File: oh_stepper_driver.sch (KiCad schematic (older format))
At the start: 22 parts, among them P2 CONN_01X02, P3 CONN_01X02, SW1 BOOT_MODE, SW2 RST, U2 STM32F446RCTx, X1 ABM8G

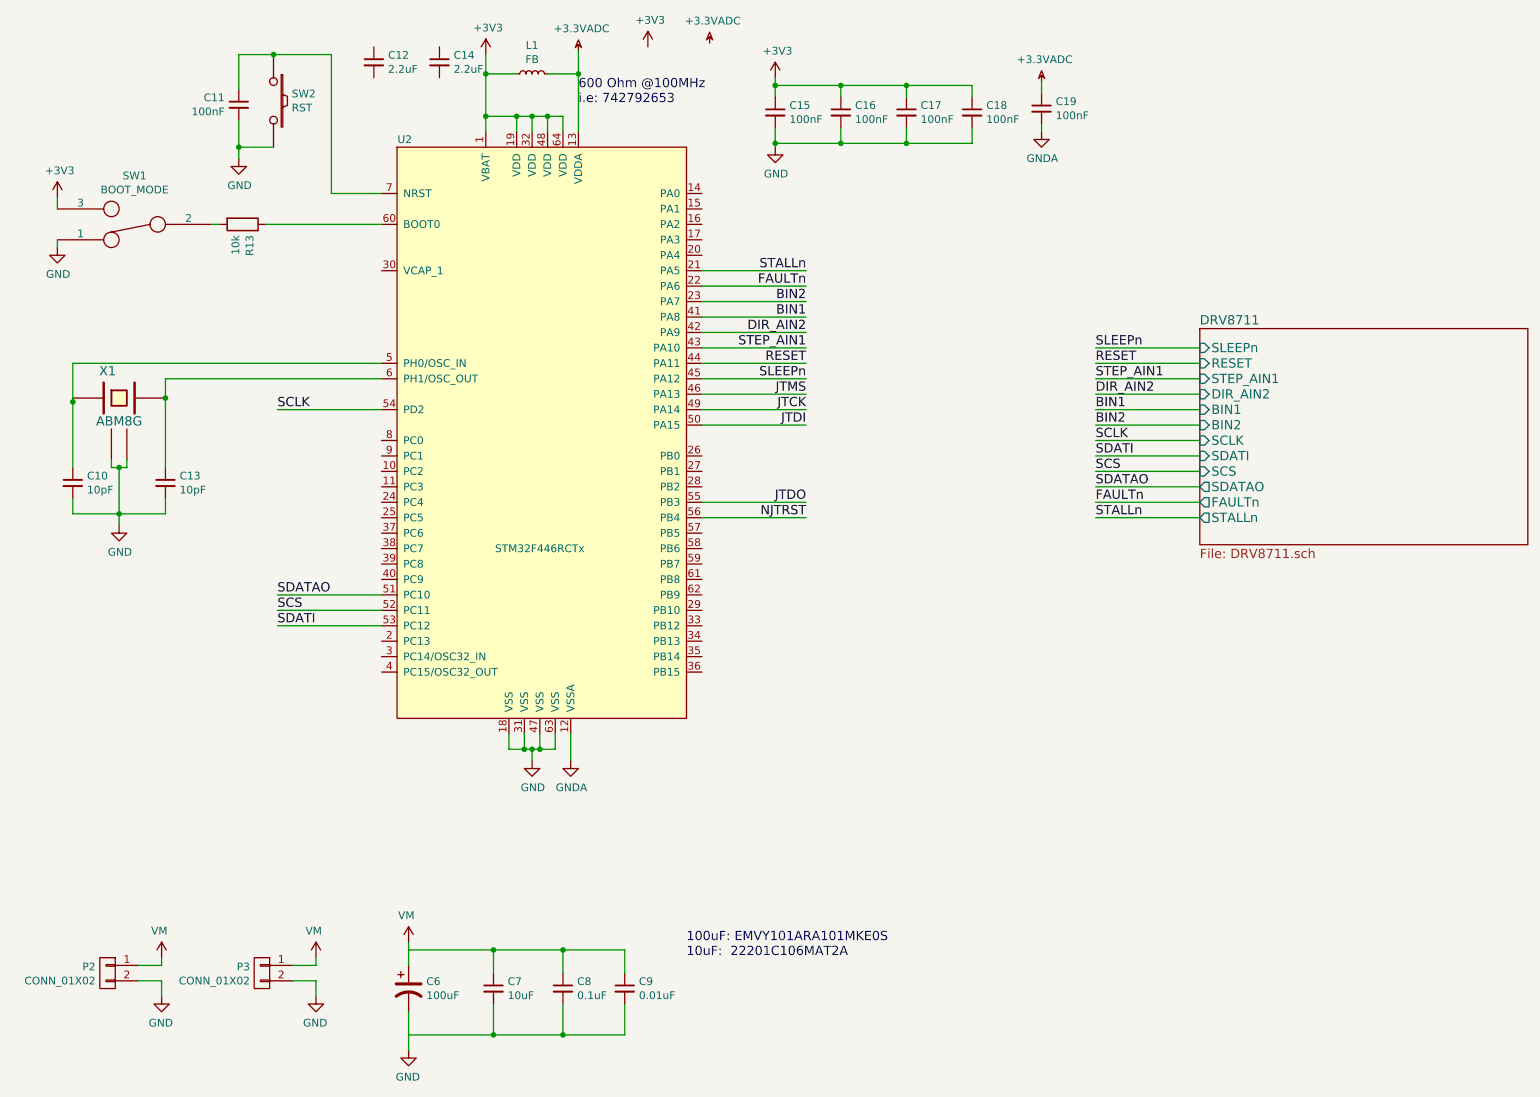
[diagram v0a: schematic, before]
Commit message: routing FETs
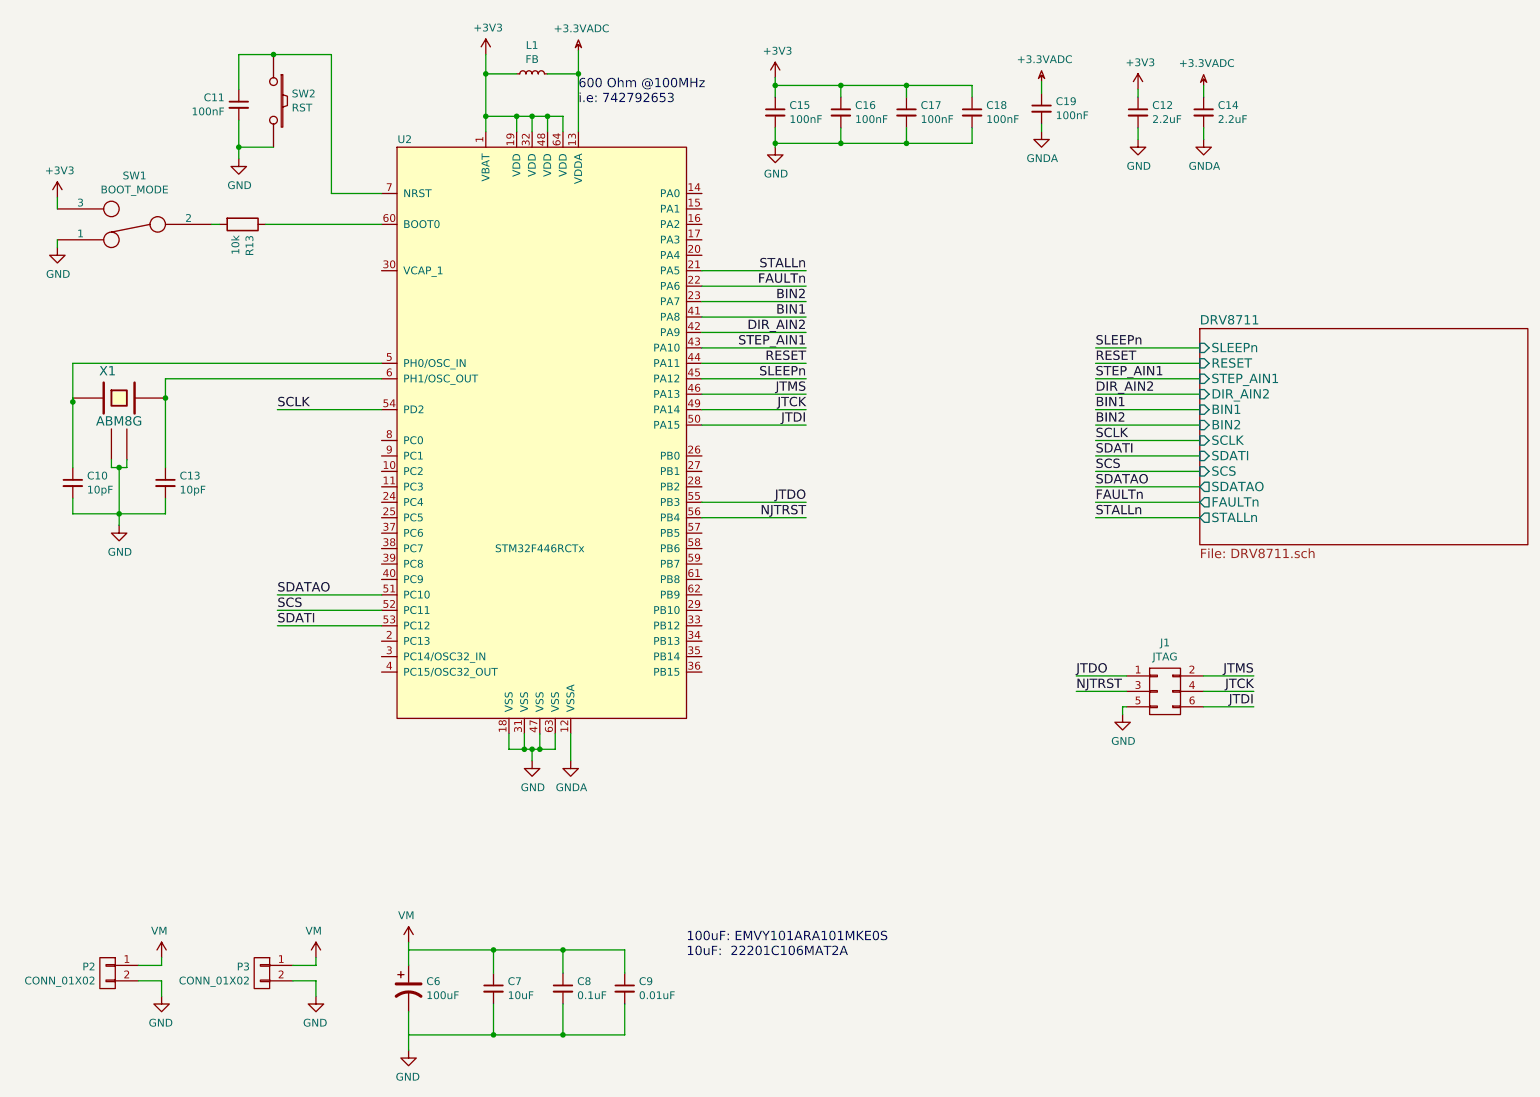
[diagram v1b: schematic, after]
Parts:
- added J1: JTAG, Pin_Headers:Pin_Header_Straight_2x03_Pitch2.54mm, symbol CONN_02X03
- SW1: footprint (none) -> Pin_Headers:Pin_Header_Straight_1x03_Pitch2.54mm
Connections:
- net +3.3VADC: now also C14.1
- net +3V3: now also C12.1
- net GND: now also C12.2, J1.5 (P5)
- net GNDA: now also C14.2
- net JTCK: now also J1.4 (P4)
- net JTDI: now also J1.6 (P6)
- net JTDO: now also J1.1 (P1)
- net JTMS: now also J1.2 (P2)
- net NJTRST: now also J1.3 (P3)
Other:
- moved on the sheet: C12, C14
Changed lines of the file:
@@
 L C_Small C12
 U 1 1 587F3123
-P 2775 1150
-F 0 "C12" H 2867 1196 50  0000 L CNN
-F 1 "2.2uF" H 2867 1105 50  0000 L CNN
-F 2 "Capacitors_SMD:C_0402" H 2867 1059 50  0001 L CNN
-F 3 "" H 2775 1150 50  0000 C CNN
-	1    2775 1150
+P 7725 1475
+F 0 "C12" H 7817 1521 50  0000 L CNN
+F 1 "2.2uF" H 7817 1430 50  0000 L CNN
+F 2 "Capacitors_SMD:C_0402" H 7817 1384 50  0001 L CNN
+F 3 "" H 7725 1475 50  0000 C CNN
+	1    7725 1475
 	1    0    0    -1
 $EndComp
@@
 L C_Small C14
 U 1 1 587F3193
-P 3200 1150
-F 0 "C14" H 3292 1196 50  0000 L CNN
-F 1 "2.2uF" H 3292 1105 50  0000 L CNN
-F 2 "Capacitors_SMD:C_0402" H 3292 1059 50  0001 L CNN
-F 3 "" H 3200 1150 50  0000 C CNN
-	1    3200 1150
+P 8150 1475
+F 0 "C14" H 8242 1521 50  0000 L CNN
+F 1 "2.2uF" H 8242 1430 50  0000 L CNN
+F 2 "Capacitors_SMD:C_0402" H 8242 1384 50  0001 L CNN
+F 3 "" H 8150 1475 50  0000 C CNN
+	1    8150 1475
 	1    0    0    -1
 $EndComp
@@
 F 0 "SW1" H 1225 1885 50  0000 C CNN
 F 1 "BOOT_MODE" H 1225 1976 50  0000 C CNN
-F 2 "" H 1225 2200 50  0001 C CNN
+F 2 "Pin_Headers:Pin_Header_Straight_1x03_Pitch2.54mm" H 1225 2200 50  0001 C CNN
 F 3 "" H 1225 2200 50  0000 C CNN
 	1    1225 2200
@@
 L +3V3 #PWR019
 U 1 1 5897DB0B
-P 4550 1050
-F 0 "#PWR019" H 4550 900 50  0001 C CNN
-F 1 "+3V3" H 4565 1223 50  0000 C CNN
-F 2 "" H 4550 1050 50  0000 C CNN
-F 3 "" H 4550 1050 50  0000 C CNN
-	1    4550 1050
+P 7725 1325
+F 0 "#PWR019" H 7725 1175 50  0001 C CNN
+F 1 "+3V3" H 7740 1498 50  0000 C CNN
+F 2 "" H 7725 1325 50  0000 C CNN
+F 3 "" H 7725 1325 50  0000 C CNN
+	1    7725 1325
 	1    0    0    -1
 $EndComp
@@
 L +3.3VADC #PWR020
 U 1 1 5897DB11
-P 4950 1025
-F 0 "#PWR020" H 5100 975 50  0001 C CNN
-F 1 "+3.3VADC" H 4970 1168 50  0000 C CNN
-F 2 "" H 4950 1025 50  0000 C CNN
-F 3 "" H 4950 1025 50  0000 C CNN
-	1    4950 1025
+P 8150 1300
+F 0 "#PWR020" H 8300 1250 50  0001 C CNN
+F 1 "+3.3VADC" H 8170 1443 50  0000 C CNN
+F 2 "" H 8150 1300 50  0000 C CNN
+F 3 "" H 8150 1300 50  0000 C CNN
+	1    8150 1300
 	1    0    0    -1
 $EndComp
@@
 Text Label 5575 4100 2    60   ~ 0
 NJTRST
+$Comp
+L CONN_02X03 J1
+U 1 1 58993DC8
+P 7900 5225
+F 0 "J1" H 7900 5540 50  0000 C CNN
+F 1 "JTAG" H 7900 5449 50  0000 C CNN
+F 2 "Pin_Headers:Pin_Header_Straight_2x03_Pitch2.54mm" H 1625 775 50  0001 C CNN
+F 3 "" H 1625 775 50  0001 C CNN
+	1    7900 5225
+	1    0    0    -1
+$EndComp
+Wire Wire Line
+	8150 5125 8475 5125
+Text Label 8475 5125 2    60   ~ 0
+JTMS
+Wire Wire Line
+	8150 5225 8475 5225
+Text Label 8475 5225 2    60   ~ 0
+JTCK
+Wire Wire Line
+	8150 5325 8475 5325
+Text Label 8475 5325 2    60   ~ 0
+JTDI
+Wire Wire Line
+	7650 5125 7325 5125
+Text Label 7325 5125 0    60   ~ 0
+JTDO
+Wire Wire Line
+	7650 5225 7325 5225
+Text Label 7325 5225 0    60   ~ 0
+NJTRST
+$Comp
+L GND #PWR021
+U 1 1 5899498D
+P 7625 5375
+F 0 "#PWR021" H 7675 5425 50  0001 C CNN
+F 1 "GND" H 7630 5202 50  0000 C CNN
+F 2 "" H 50  -25 50  0001 C CNN
+F 3 "" H 50  -25 50  0001 C CNN
+	1    7625 5375
+	1    0    0    -1
+$EndComp
+Wire Wire Line
+	7650 5325 7625 5325
+Wire Wire Line
+	7625 5325 7625 5375
+$Comp
+L GNDA #PWR?
+U 1 1 58995E10
+P 8150 1650
+F 0 "#PWR?" H 8150 1400 50  0001 C CNN
+F 1 "GNDA" H 8155 1477 50  0000 C CNN
+F 2 "" H 8150 1650 50  0000 C CNN
+F 3 "" H 8150 1650 50  0000 C CNN
+	1    8150 1650
+	1    0    0    -1
+$EndComp
+$Comp
+L GND #PWR?
+U 1 1 58995E53
+P 7725 1650
+F 0 "#PWR?" H -25 -300 50  0001 C CNN
+F 1 "GND" H 7730 1477 50  0000 C CNN
+F 2 "" H -25 -50 50  0001 C CNN
+F 3 "" H -25 -50 50  0001 C CNN
+	1    7725 1650
+	1    0    0    -1
+$EndComp
+Wire Wire Line
+	8150 1300 8150 1375
+Wire Wire Line
+	7725 1325 7725 1375
+Wire Wire Line
+	7725 1575 7725 1650
+Wire Wire Line
+	8150 1650 8150 1575
 $EndSCHEMATC

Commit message: 4 layers
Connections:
- net GND: now also P2.1 (P1), P3.1 (P1); no longer P2.2 (P2), P3.2 (P2)
- net VM: now also P2.2 (P2), P3.2 (P2); no longer P2.1 (P1), P3.1 (P1)
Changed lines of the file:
@@
 F 3 "" H 1050 7050 50  0000 C CNN
 	1    1050 7050
-	-1   0    0    -1
+	-1   0    0    1
 $EndComp
 $Comp
@@
 F 3 "" H 2050 7050 50  0000 C CNN
 	1    2050 7050
-	-1   0    0    -1
+	-1   0    0    1
 $EndComp
 $Comp

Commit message: library of transeiver can
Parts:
- added U?: TJA1050, symbol TJA1050
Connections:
- net GND: now also C7.2, C8.2, C9.2
- net VM: now also C7.1, C8.1, C9.1
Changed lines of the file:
@@
 LIBS:contrib
 LIBS:valves
+LIBS:tja1050
 LIBS:oh_stepper_driver-cache
 EELAYER 26 0
@@
 $EndDescr
 $Comp
-L GND #PWR01
+L GND #PWR5
 U 1 1 587AE5B3
 P 1400 7200
-F 0 "#PWR01" H 1400 6950 50  0001 C CNN
+F 0 "#PWR5" H 1400 6950 50  0001 C CNN
 F 1 "GND" H 1405 7027 50  0000 C CNN
 F 2 "" H 1400 7200 50  0000 C CNN
@@
 $EndComp
 $Comp
-L VM #PWR02
+L VM #PWR4
 U 1 1 587AE5B4
 P 1400 6950
-F 0 "#PWR02" H 1400 6800 50  0001 C CNN
+F 0 "#PWR4" H 1400 6800 50  0001 C CNN
 F 1 "VM" H 1415 7123 50  0000 C CNN
 F 2 "" H 1400 6950 50  0000 C CNN
@@
 $EndComp
 $Comp
-L GND #PWR03
+L GND #PWR8
 U 1 1 587BB2AD
 P 2400 7200
-F 0 "#PWR03" H 2400 6950 50  0001 C CNN
+F 0 "#PWR8" H 2400 6950 50  0001 C CNN
 F 1 "GND" H 2405 7027 50  0000 C CNN
 F 2 "" H 2400 7200 50  0000 C CNN
@@
 $EndComp
 $Comp
-L VM #PWR04
+L VM #PWR7
 U 1 1 587BB2B3
 P 2400 6950
-F 0 "#PWR04" H 2400 6800 50  0001 C CNN
+F 0 "#PWR7" H 2400 6800 50  0001 C CNN
 F 1 "VM" H 2415 7123 50  0000 C CNN
 F 2 "" H 2400 6950 50  0000 C CNN
@@
 $EndComp
 $Comp
-L GND #PWR05
+L GND #PWR10
 U 1 1 587BC837
 P 3000 7550
-F 0 "#PWR05" H 3000 7300 50  0001 C CNN
+F 0 "#PWR10" H 3000 7300 50  0001 C CNN
 F 1 "GND" H 3005 7377 50  0000 C CNN
 F 2 "" H 3000 7550 50  0000 C CNN
@@
 $EndComp
 $Comp
-L VM #PWR06
+L VM #PWR9
 U 1 1 587BC83D
 P 3000 6850
-F 0 "#PWR06" H 3000 6700 50  0001 C CNN
+F 0 "#PWR9" H 3000 6700 50  0001 C CNN
 F 1 "VM" H 3015 7023 50  0000 C CNN
 F 2 "" H 3000 6850 50  0000 C CNN
@@
 $EndComp
 $Comp
-L GND #PWR07
+L GND #PWR3
 U 1 1 587F3A6D
 P 1125 4150
-F 0 "#PWR07" H 1125 3900 50  0001 C CNN
+F 0 "#PWR3" H 1125 3900 50  0001 C CNN
 F 1 "GND" H 1130 3977 50  0000 C CNN
 F 2 "" H 1125 4150 50  0000 C CNN
@@
 $EndComp
 $Comp
-L GND #PWR08
+L GND #PWR12
 U 1 1 587F4021
 P 3800 5675
-F 0 "#PWR08" H 3800 5425 50  0001 C CNN
+F 0 "#PWR12" H 3800 5425 50  0001 C CNN
 F 1 "GND" H 3805 5502 50  0000 C CNN
 F 2 "" H 3800 5675 50  0000 C CNN
@@
 $EndComp
 $Comp
-L +3V3 #PWR09
+L +3V3 #PWR11
 U 1 1 587F4D80
 P 3500 1100
-F 0 "#PWR09" H 3500 950 50  0001 C CNN
+F 0 "#PWR11" H 3500 950 50  0001 C CNN
 F 1 "+3V3" H 3515 1273 50  0000 C CNN
 F 2 "" H 3500 1100 50  0000 C CNN
@@
 $EndComp
 $Comp
-L +3V3 #PWR010
+L +3V3 #PWR15
 U 1 1 587F53E0
 P 5375 1250
-F 0 "#PWR010" H 5375 1100 50  0001 C CNN
+F 0 "#PWR15" H 5375 1100 50  0001 C CNN
 F 1 "+3V3" H 5390 1423 50  0000 C CNN
 F 2 "" H 5375 1250 50  0000 C CNN
@@
 $EndComp
 $Comp
-L GND #PWR011
+L GND #PWR16
 U 1 1 587F53FA
 P 5375 1700
-F 0 "#PWR011" H 5375 1450 50  0001 C CNN
+F 0 "#PWR16" H 5375 1450 50  0001 C CNN
 F 1 "GND" H 5380 1527 50  0000 C CNN
 F 2 "" H 5375 1700 50  0000 C CNN
@@
 	4400 6900 4400 7050
 Wire Wire Line
-	3000 6900 4400 6900
-Wire Wire Line
 	3000 6850 3000 7000
 Wire Wire Line
@@
 Wire Wire Line
 	3000 7300 3000 7550
-Wire Wire Line
-	3000 7450 4400 7450
 Wire Wire Line
 	4400 7450 4400 7250
@@
 $EndComp
 $Comp
-L +3.3VADC #PWR012
+L +3.3VADC #PWR17
 U 1 1 587F5AA0
 P 7100 1275
-F 0 "#PWR012" H 7250 1225 50  0001 C CNN
+F 0 "#PWR17" H 7250 1225 50  0001 C CNN
 F 1 "+3.3VADC" H 7120 1418 50  0000 C CNN
 F 2 "" H 7100 1275 50  0000 C CNN
@@
 $EndComp
 $Comp
-L GNDA #PWR013
+L GNDA #PWR18
 U 1 1 587F5ADA
 P 7100 1600
-F 0 "#PWR013" H 7100 1350 50  0001 C CNN
+F 0 "#PWR18" H 7100 1350 50  0001 C CNN
 F 1 "GNDA" H 7105 1427 50  0000 C CNN
 F 2 "" H 7100 1600 50  0000 C CNN
@@
 	7100 1550 7100 1600
 $Comp
-L +3.3VADC #PWR014
+L +3.3VADC #PWR14
 U 1 1 587F5C3A
 P 4100 1075
-F 0 "#PWR014" H 4250 1025 50  0001 C CNN
+F 0 "#PWR14" H 4250 1025 50  0001 C CNN
 F 1 "+3.3VADC" H 4120 1218 50  0000 C CNN
 F 2 "" H 4100 1075 50  0000 C CNN
@@
 Connection ~ 3800 5600
 $Comp
-L GNDA #PWR015
+L GNDA #PWR13
 U 1 1 587F63C7
 P 4050 5675
-F 0 "#PWR015" H 4050 5425 50  0001 C CNN
+F 0 "#PWR13" H 4050 5425 50  0001 C CNN
 F 1 "GNDA" H 4055 5502 50  0000 C CNN
 F 2 "" H 4050 5675 50  0000 C CNN
@@
 $EndComp
 $Comp
-L +3V3 #PWR016
+L +3V3 #PWR1
 U 1 1 5897C965
 P 725 2025
-F 0 "#PWR016" H 725 1875 50  0001 C CNN
+F 0 "#PWR1" H 725 1875 50  0001 C CNN
 F 1 "+3V3" H 740 2198 50  0000 C CNN
 F 2 "" H 725 2025 50  0000 C CNN
@@
 $EndComp
 $Comp
-L GND #PWR017
+L GND #PWR2
 U 1 1 5897C9DD
 P 725 2350
-F 0 "#PWR017" H 725 2100 50  0001 C CNN
+F 0 "#PWR2" H 725 2100 50  0001 C CNN
 F 1 "GND" H 730 2177 50  0000 C CNN
 F 2 "" H 725 2350 50  0000 C CNN
@@
 $EndComp
 $Comp
-L GND #PWR018
+L GND #PWR6
 U 1 1 5897E497
 P 1900 1775
-F 0 "#PWR018" H 1900 1525 50  0001 C CNN
+F 0 "#PWR6" H 1900 1525 50  0001 C CNN
 F 1 "GND" H 1905 1602 50  0000 C CNN
 F 2 "" H 1900 1775 50  0000 C CNN
@@
 $EndComp
 $Comp
-L +3V3 #PWR019
+L +3V3 #PWR20
 U 1 1 5897DB0B
 P 7725 1325
-F 0 "#PWR019" H 7725 1175 50  0001 C CNN
+F 0 "#PWR20" H 7725 1175 50  0001 C CNN
 F 1 "+3V3" H 7740 1498 50  0000 C CNN
 F 2 "" H 7725 1325 50  0000 C CNN
@@
 $EndComp
 $Comp
-L +3.3VADC #PWR020
+L +3.3VADC #PWR22
 U 1 1 5897DB11
 P 8150 1300
-F 0 "#PWR020" H 8300 1250 50  0001 C CNN
+F 0 "#PWR22" H 8300 1250 50  0001 C CNN
 F 1 "+3.3VADC" H 8170 1443 50  0000 C CNN
 F 2 "" H 8150 1300 50  0000 C CNN
@@
 NJTRST
 $Comp
-L GND #PWR021
+L GND #PWR19
 U 1 1 5899498D
 P 7625 5375
-F 0 "#PWR021" H 7675 5425 50  0001 C CNN
+F 0 "#PWR19" H 7675 5425 50  0001 C CNN
 F 1 "GND" H 7630 5202 50  0000 C CNN
 F 2 "" H 50  -25 50  0001 C CNN
@@
 	7625 5325 7625 5375
 $Comp
-L GNDA #PWR?
+L GNDA #PWR23
 U 1 1 58995E10
 P 8150 1650
-F 0 "#PWR?" H 8150 1400 50  0001 C CNN
+F 0 "#PWR23" H 8150 1400 50  0001 C CNN
 F 1 "GNDA" H 8155 1477 50  0000 C CNN
 F 2 "" H 8150 1650 50  0000 C CNN
@@
 $EndComp
 $Comp
-L GND #PWR?
+L GND #PWR21
 U 1 1 58995E53
 P 7725 1650
-F 0 "#PWR?" H -25 -300 50  0001 C CNN
+F 0 "#PWR21" H -25 -300 50  0001 C CNN
 F 1 "GND" H 7730 1477 50  0000 C CNN
 F 2 "" H -25 -50 50  0001 C CNN
@@
 Wire Wire Line
 	8150 1650 8150 1575
+Wire Wire Line
+	3000 6900 4400 6900
+Connection ~ 3000 6900
+Wire Wire Line
+	3000 7450 4400 7450
+Connection ~ 3000 7450
+$Comp
+L TJA1050 U?
+U 1 1 58A846F4
+P 6350 5450
+F 0 "U?" H 6375 4806 60  0000 C CNN
+F 1 "TJA1050" H 6375 4700 60  0000 C CNN
+F 2 "" H 650 500 60  0001 C CNN
+F 3 "" H 650 500 60  0001 C CNN
+	1    6350 5450
+	1    0    0    -1
+$EndComp
 $EndSCHEMATC

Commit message: encoder placement
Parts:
- added U4: AS5047D, SMD_Packages:SSOP-14, symbol AS5047D
- U3: renamed from U?; footprint (none) -> SMD_Packages:SOIC-8-N
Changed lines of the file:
@@
 LIBS:valves
 LIBS:tja1050
+LIBS:as5047d
 LIBS:oh_stepper_driver-cache
 EELAYER 26 0
@@
 Connection ~ 3000 7450
 $Comp
-L TJA1050 U?
+L TJA1050 U3
 U 1 1 58A846F4
 P 6350 5450
-F 0 "U?" H 6375 4806 60  0000 C CNN
+F 0 "U3" H 6375 4806 60  0000 C CNN
 F 1 "TJA1050" H 6375 4700 60  0000 C CNN
-F 2 "" H 650 500 60  0001 C CNN
+F 2 "SMD_Packages:SOIC-8-N" H 650 500 60  0001 C CNN
 F 3 "" H 650 500 60  0001 C CNN
 	1    6350 5450
 	1    0    0    -1
 $EndComp
+$Comp
+L AS5047D U4
+U 1 1 58AA2264
+P 9350 5525
+F 0 "U4" H 9350 6112 60  0000 C CNN
+F 1 "AS5047D" H 9350 6006 60  0000 C CNN
+F 2 "SMD_Packages:SSOP-14" H 75  0   60  0001 C CNN
+F 3 "" H 75  0   60  0001 C CNN
+	1    9350 5525
+	1    0    0    -1
+$EndComp

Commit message: KiCAD version updated
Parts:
- C10, C11, C12, C13, C14, C15, C16, C17, C18, C19, C7, C8, C9: symbol C_Small -> oh_stepper_driver-rescue:C_Small
- C6: symbol CP1 -> oh_stepper_driver-rescue:CP1
- J1: symbol CONN_02X03 -> oh_stepper_driver-rescue:CONN_02X03
- L1: symbol L_Small -> oh_stepper_driver-rescue:L_Small
- P2, P3: symbol CONN_01X02 -> oh_stepper_driver-rescue:CONN_01X02
- R13: symbol R -> oh_stepper_driver-rescue:R
- SW1: symbol SWITCH_INV -> oh_stepper_driver-rescue:SWITCH_INV
- SW2: symbol SW_PUSH -> oh_stepper_driver-rescue:SW_PUSH
- U2: symbol STM32F446RCTx -> stm32f446_lqfp64:STM32F446RCTx
- U3: symbol TJA1050 -> tja1050:TJA1050
- U4: symbol AS5047D -> as5047d:AS5047D
- X1: symbol ABM8G -> abm8g:ABM8G
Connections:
- net at C10.1, U2.5 (PH0/OSC_IN): no longer X1.1
